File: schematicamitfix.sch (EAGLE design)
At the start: 41 parts, among them J1 FTDI_DEVICE, M1 WIRELESS-NRF24L01, U1 ATMEGA328P_TQFP, U2 GY-521MPU6050, U3 MAX1595EUA33+

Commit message: Saved fixed schematic
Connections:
- removed net N$15: U3.GND, U3.PGND
- removed net N$16: R9.1
- removed net N$18: U$8.S
- removed net N$19: C11.1, U3.AOUT, U3.OUT
- removed net N$20: C13.1, U$19.-
- removed net N$22: R5.1
- removed net N$28: U$5.S
- removed net N$29: R3.1
- removed net N$3: R4.1
- removed net N$30: U$9.S
- removed net N$31: R2.1
- removed net N$32: U$12.S
- removed net N$33: LED1.C
- removed net N$4: C5.2, C6.2, M1.GND
- removed net N$8: C7.2, C8.2
- net AVCC: no longer C4.1
- net GND: now also C11.2, C13.1, C4.2, C5.2, C6.2, C7.2, C8.2, C9.2, LED1.C, M1.GND, R2.1, R3.1, R4.1, R5.1, R9.1, U$12.S, U$19.-, U$5.S, U$8.S, U$9.S, U3.GND, U3.PGND
- net N$1: now also U1.PC6(/RESET)
- net N$10: now also C10.2
- net N$6: now also C10.1
- net VCC: now also C11.1, C4.1, U3.AOUT, U3.OUT
- net VIN: now also C9.1

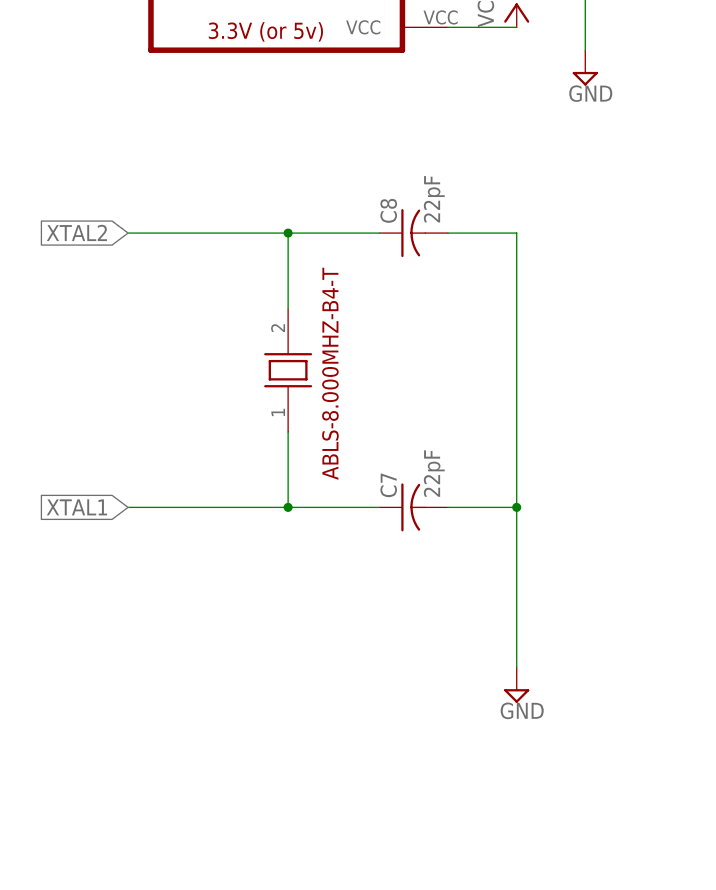
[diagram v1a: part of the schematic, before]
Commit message: Switched from crystal oscillator to ceramic resonator
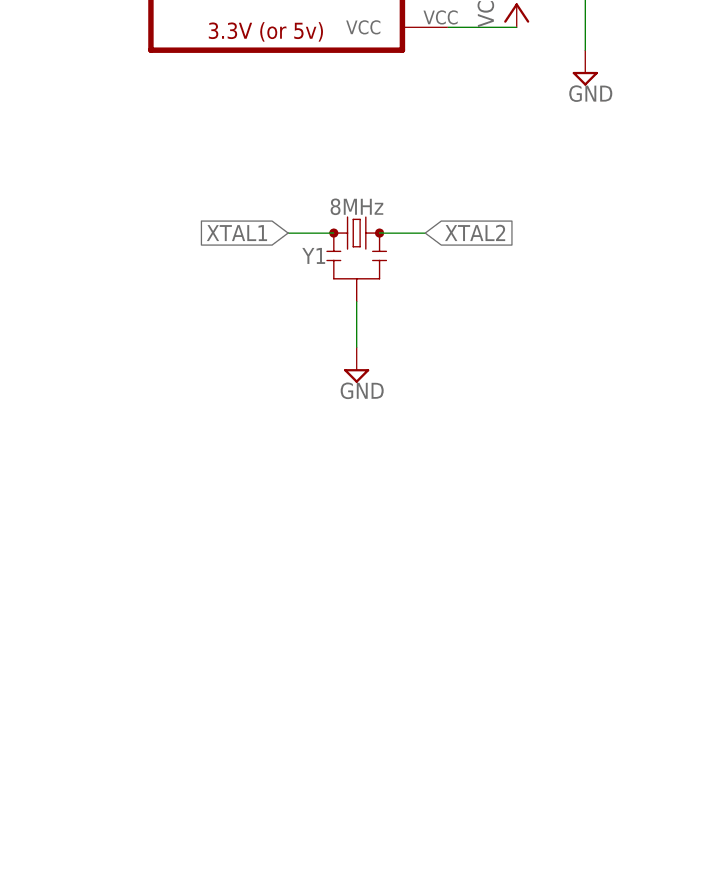
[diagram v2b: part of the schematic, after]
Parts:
- removed C7, C8: 22pF, rcl:C-USC0603
- removed U$1: ABLS-8.000MHZ-B4-T, ABLS-8.000MHZ-B4-T:ABLS-8.000MHZ-B4-T
- added Y1: 8MHz, SparkFun-Clocks:RESONATOR-8MHZSMD_3.2X1.3
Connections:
- net GND: now also Y1.2; no longer C7.2, C8.2
- net XTAL1: now also Y1.1; no longer C7.1, U$1.1
- net XTAL2: now also Y1.3; no longer C8.1, U$1.2
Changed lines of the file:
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@@
 <part name="LED1" library="LilyPad-Wearables" deviceset="LED" device="1206"/>
 <part name="R6" library="SparkFun" deviceset="RESISTOR" device="0603-RES" value="100 ohms"/>
-<part name="C7" library="rcl" library_urn="urn:adsk.eagle:library:334" deviceset="C-US" device="C0603" package3d_urn="urn:adsk.eagle:package:23616/2" value="22pF"/>
-<part name="C8" library="rcl" library_urn="urn:adsk.eagle:library:334" deviceset="C-US" device="C0603" package3d_urn="urn:adsk.eagle:package:23616/2" value="22pF"/>
-<part name="SUPPLY9" library="supply2" library_urn="urn:adsk.eagle:library:372" deviceset="GND" device=""/>
 <part name="U$19" library="quad" deviceset="JST_CONNECTOR_FEMALE" device=""/>
 <part name="SUPPLY15" library="supply2" library_urn="urn:adsk.eagle:library:372" deviceset="GND" device=""/>
@@
 <part name="SUPPLY30" library="supply2" library_urn="urn:adsk.eagle:library:372" deviceset="GND" device=""/>
 <part name="SUPPLY31" library="supply2" library_urn="urn:adsk.eagle:library:372" deviceset="GND" device=""/>
-<part name="U$1" library="ABLS-8.000MHZ-B4-T" deviceset="ABLS-8.000MHZ-B4-T" device=""/>
 <part name="U3" library="MAX1595EUA33+" deviceset="MAX1595EUA33+" device=""/>
 <part name="SUPPLY10" library="supply2" library_urn="urn:adsk.eagle:library:372" deviceset="GND" device=""/>
@@
 <part name="U$9" library="quad" deviceset="N-CHANNEL-MOSFET" device="-IRLML6244TRPBF"/>
 <part name="U$12" library="quad" deviceset="N-CHANNEL-MOSFET" device="-IRLML6244TRPBF"/>
+<part name="Y1" library="SparkFun-Clocks" deviceset="RESONATOR-8MHZ" device="SMD_3.2X1.3" value="8MHz"/>
+<part name="SUPPLY13" library="supply2" library_urn="urn:adsk.eagle:library:372" deviceset="GND" device=""/>
 </parts>
 <sheets>
@@
 <instance part="LED1" gate="G$1" x="111.76" y="10.16"/>
 <instance part="R6" gate="G$1" x="111.76" y="20.32" rot="R90"/>
-<instance part="C7" gate="G$1" x="-33.02" y="-45.72" rot="R90"/>
-<instance part="C8" gate="G$1" x="-33.02" y="-15.24" rot="R90"/>
-<instance part="SUPPLY9" gate="GND" x="-20.32" y="-66.04"/>
 <instance part="U$19" gate="G$1" x="17.78" y="134.62" rot="R90"/>
 <instance part="SUPPLY15" gate="GND" x="5.08" y="119.38"/>
@@
 <instance part="SUPPLY30" gate="GND" x="162.56" y="-281.94"/>
 <instance part="SUPPLY31" gate="GND" x="111.76" y="-2.54"/>
-<instance part="U$1" gate="ABLS-8.000MHZ-B4-T" x="-45.72" y="-30.48" rot="R90"/>
 <instance part="U3" gate="A" x="66.04" y="129.54"/>
 <instance part="SUPPLY10" gate="GND" x="60.96" y="109.22"/>
@@
 <instance part="U$9" gate="G$1" x="246.38" y="25.4"/>
 <instance part="U$12" gate="G$1" x="276.86" y="165.1"/>
+<instance part="Y1" gate="G$1" x="-38.1" y="-15.24"/>
+<instance part="SUPPLY13" gate="GND" x="-38.1" y="-30.48"/>
 </instances>
 <busses>
@@
 <pinref part="SUPPLY19" gate="GND" pin="GND"/>
 <pinref part="SUPPLY30" gate="GND" pin="GND"/>
-</segment>
-<segment>
-<pinref part="C7" gate="G$1" pin="2"/>
-<wire x1="-20.32" y1="-45.72" x2="-27.94" y2="-45.72" width="0.1524" layer="91"/>
-<wire x1="-20.32" y1="-45.72" x2="-20.32" y2="-63.5" width="0.1524" layer="91"/>
-<junction x="-20.32" y="-45.72"/>
-<pinref part="C8" gate="G$1" pin="2"/>
-<wire x1="-27.94" y1="-15.24" x2="-20.32" y2="-15.24" width="0.1524" layer="91"/>
-<wire x1="-20.32" y1="-15.24" x2="-20.32" y2="-45.72" width="0.1524" layer="91"/>
-<pinref part="SUPPLY9" gate="GND" pin="GND"/>
 </segment>
 <segment>
@@
 <pinref part="SUPPLY16" gate="GND" pin="GND"/>
 <pinref part="SUPPLY23" gate="GND" pin="GND"/>
+</segment>
+<segment>
+<pinref part="Y1" gate="G$1" pin="2"/>
+<wire x1="-38.1" y1="-22.86" x2="-38.1" y2="-27.94" width="0.1524" layer="91"/>
+<pinref part="SUPPLY13" gate="GND" pin="GND"/>
 </segment>
 </net>
@@
 <net name="XTAL2" class="0">
 <segment>
-<wire x1="-63.5" y1="-15.24" x2="-45.72" y2="-15.24" width="0.1524" layer="91"/>
-<pinref part="C8" gate="G$1" pin="1"/>
-<label x="-63.5" y="-15.24" size="1.778" layer="95" rot="R180" xref="yes"/>
-<pinref part="U$1" gate="ABLS-8.000MHZ-B4-T" pin="2"/>
-<wire x1="-45.72" y1="-15.24" x2="-35.56" y2="-15.24" width="0.1524" layer="91"/>
-<wire x1="-45.72" y1="-23.622" x2="-45.72" y2="-15.24" width="0.1524" layer="91"/>
-<junction x="-45.72" y="-15.24"/>
-</segment>
-<segment>
 <pinref part="U1" gate="U$1" pin="PB7(XTAL2/TOSC2)"/>
 <wire x1="38.1" y1="38.1" x2="35.56" y2="38.1" width="0.1524" layer="91"/>
 <label x="35.56" y="38.1" size="1.778" layer="95" rot="R270" xref="yes"/>
 </segment>
+<segment>
+<pinref part="Y1" gate="G$1" pin="3"/>
+<wire x1="-35.56" y1="-15.24" x2="-30.48" y2="-15.24" width="0.1524" layer="91"/>
+<label x="-30.48" y="-15.24" size="1.778" layer="95" xref="yes"/>
+</segment>
 </net>
 <net name="XTAL1" class="0">
-<segment>
-<pinref part="C7" gate="G$1" pin="1"/>
-<label x="-63.5" y="-45.72" size="1.778" layer="95" rot="R180" xref="yes"/>
-<wire x1="-35.56" y1="-45.72" x2="-45.72" y2="-45.72" width="0.1524" layer="91"/>
-<pinref part="U$1" gate="ABLS-8.000MHZ-B4-T" pin="1"/>
-<wire x1="-45.72" y1="-45.72" x2="-63.5" y2="-45.72" width="0.1524" layer="91"/>
-<wire x1="-45.72" y1="-37.338" x2="-45.72" y2="-45.72" width="0.1524" layer="91"/>
-<junction x="-45.72" y="-45.72"/>
-</segment>
 <segment>
 <pinref part="U1" gate="U$1" pin="PB6(XTAL1/TOSC1)"/>
@@
 <label x="35.56" y="43.18" size="1.778" layer="95" rot="R90" xref="yes"/>
 </segment>
-</net>
+<segment>
+<pinref part="Y1" gate="G$1" pin="1"/>
+<wire x1="-40.64" y1="-15.24" x2="-45.72" y2="-15.24" width="0.1524" layer="91"/>
+<label x="-45.72" y="-15.24" size="1.778" layer="95" rot="R180" xref="yes"/>
+</segment>
+</net>
